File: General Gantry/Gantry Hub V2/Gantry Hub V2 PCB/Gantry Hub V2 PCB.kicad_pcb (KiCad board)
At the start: 4 copper layers, 140 x 85 mm, 44 parts, among them J1 Conn_01x02_Socket, J2 178-025-513R571, J3 DIN-8, J4 DIN-4, J5 DIN-4, J6 178-025-513R571, U1 TPIC6B595N, U10 TPIC6B595N, U11 TPIC6B595N, U12 TPIC6B595N, U13 TPIC6B595N, U2 SC0915, U3 LM2575-5.0WT, U4 TPIC6B595N, U5 LM358, U6 MCP4802, U7 SN74AHCT125N, U8 TPIC6B595N, U9 TPIC6B595N

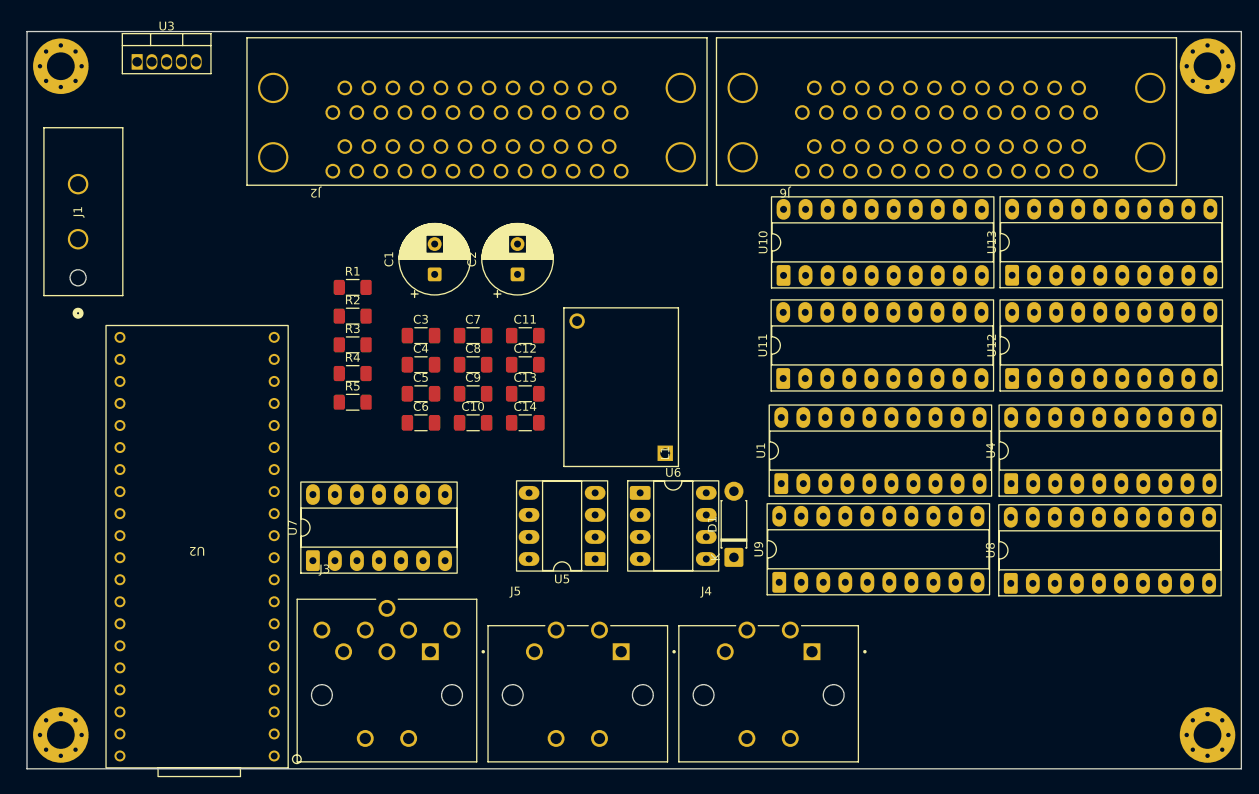
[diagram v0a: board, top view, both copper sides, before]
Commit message: Finalizes GH V2 part placement, about 60-75 percent done with routing
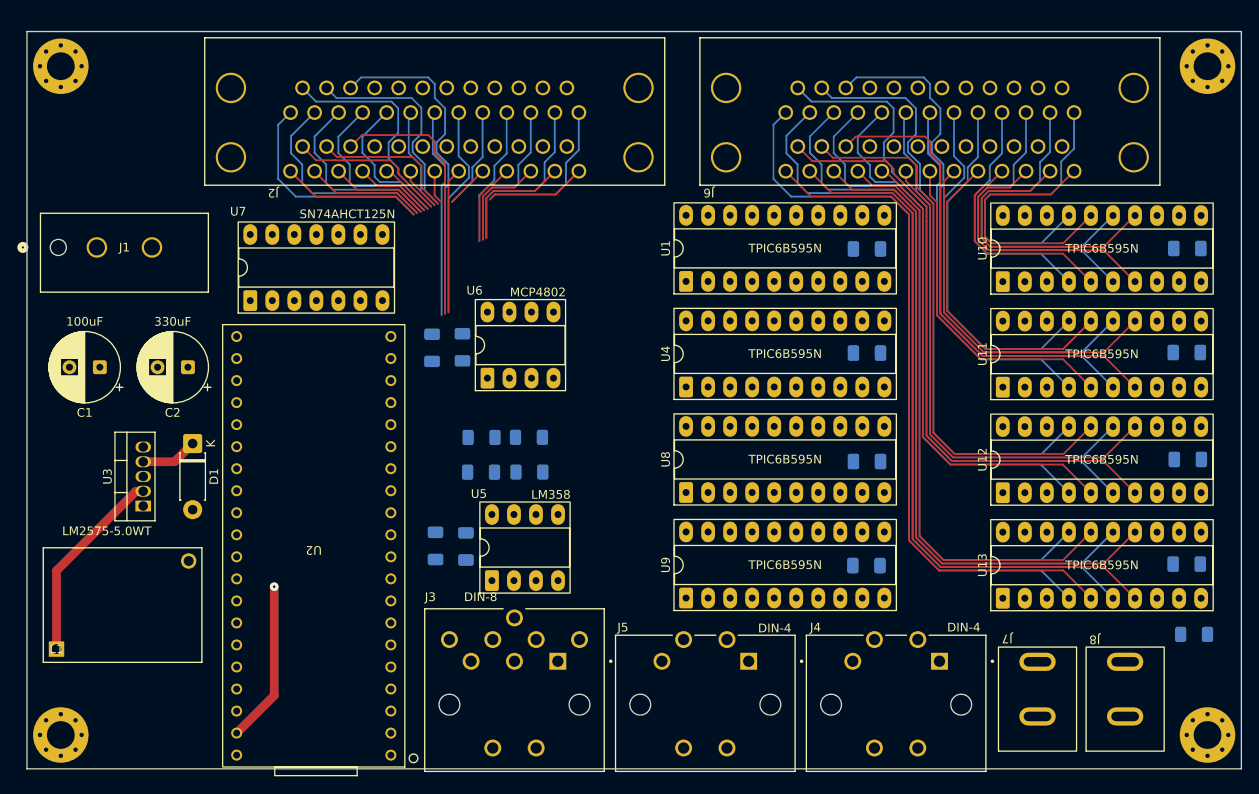
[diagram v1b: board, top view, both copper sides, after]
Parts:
- added J7: Barrel_Jack, lib_footprints:CUI PJ-037A, F.Cu at (172.5, 123.0)
- added J8: Barrel_Jack, lib_footprints:CUI PJ-037A, F.Cu at (182.6, 123.0)
- C10, C11, C12, C13, C14, C3, C4, C5, C6, C7, C8, C9, R1, R2, R3, R4, R5: moved to B.Cu
- moved R1 104.9 mm to (190.6, 113.5), turned to 180 degrees
- moved C14 78.0 mm to (189.7, 105.4), turned to 180 degrees
- moved C11 77.0 mm to (189.8, 69.0), turned to 180 degrees
- moved C13 76.8 mm to (189.8, 93.3), turned to 180 degrees
- moved C12 76.3 mm to (189.7, 81.0), turned to 180 degrees
- moved L1 73.7 mm to (59.4, 115.2), turned to 0 degrees
- moved D1 63.8 mm to (75.1, 91.5), turned to -90 degrees
- moved C3 52.4 mm to (152.8, 69.1), turned to 180 degrees
- moved C4 51.4 mm to (152.8, 81.1), turned to 180 degrees
- moved U3 51.2 mm to (69.4, 98.7), turned to 90 degrees
- moved C10 48.2 mm to (152.8, 105.6), turned to 180 degrees
- moved C9 46.1 mm to (152.8, 93.6), turned to 180 degrees
- moved C1 40.1 mm to (64.4, 82.7), turned to 180 degrees
- moved C2 39.5 mm to (74.6, 82.7), turned to 180 degrees
- moved U4 39.1 mm to (132.0, 85.0)
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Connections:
- U10 pad 14: /Valve Block Interface/CHANNEL_37 -> /Valve Block Interface/CHANNEL_44
- U10 pad 15: /Valve Block Interface/CHANNEL_38 -> /Valve Block Interface/CHANNEL_60
- U10 pad 16: /Valve Block Interface/CHANNEL_39 -> /Valve Block Interface/CHANNEL_45
- U10 pad 17: /Valve Block Interface/CHANNEL_40 -> /Valve Block Interface/CHANNEL_61
- U10 pad 4: /Valve Block Interface/CHANNEL_33 -> /Valve Block Interface/CHANNEL_58
- U10 pad 5: /Valve Block Interface/CHANNEL_34 -> /Valve Block Interface/CHANNEL_42
- U10 pad 6: /Valve Block Interface/CHANNEL_35 -> /Valve Block Interface/CHANNEL_59
- U10 pad 7: /Valve Block Interface/CHANNEL_36 -> /Valve Block Interface/CHANNEL_43
- U11 pad 14: /Valve Block Interface/CHANNEL_45 -> /Valve Block Interface/CHANNEL_40
- U11 pad 15: /Valve Block Interface/CHANNEL_46 -> /Valve Block Interface/CHANNEL_56
- U11 pad 16: /Valve Block Interface/CHANNEL_47 -> /Valve Block Interface/CHANNEL_41
- U11 pad 17: /Valve Block Interface/CHANNEL_48 -> /Valve Block Interface/CHANNEL_57
- U11 pad 4: /Valve Block Interface/CHANNEL_41 -> /Valve Block Interface/CHANNEL_55
- U11 pad 5: /Valve Block Interface/CHANNEL_42 -> /Valve Block Interface/CHANNEL_39
- U11 pad 6: /Valve Block Interface/CHANNEL_43 -> /Valve Block Interface/CHANNEL_64
- U11 pad 7: /Valve Block Interface/CHANNEL_44 -> /Valve Block Interface/CHANNEL_48
- U12 pad 14: /Valve Block Interface/CHANNEL_53 -> /Valve Block Interface/CHANNEL_38
- U12 pad 16: /Valve Block Interface/CHANNEL_55 -> /Valve Block Interface/CHANNEL_47
- U12 pad 17: /Valve Block Interface/CHANNEL_56 -> /Valve Block Interface/CHANNEL_63
- U12 pad 4: /Valve Block Interface/CHANNEL_49 -> /Valve Block Interface/CHANNEL_53
- U12 pad 5: /Valve Block Interface/CHANNEL_50 -> /Valve Block Interface/CHANNEL_37
- U12 pad 6: /Valve Block Interface/CHANNEL_51 -> /Valve Block Interface/CHANNEL_62
- U12 pad 7: /Valve Block Interface/CHANNEL_52 -> /Valve Block Interface/CHANNEL_46
- U13 pad 14: /Valve Block Interface/CHANNEL_61 -> /Valve Block Interface/CHANNEL_35
- U13 pad 15: /Valve Block Interface/CHANNEL_62 -> /Valve Block Interface/CHANNEL_51
- U13 pad 16: /Valve Block Interface/CHANNEL_63 -> /Valve Block Interface/CHANNEL_36
- U13 pad 17: /Valve Block Interface/CHANNEL_64 -> /Valve Block Interface/CHANNEL_52
- U13 pad 4: /Valve Block Interface/CHANNEL_57 -> /Valve Block Interface/CHANNEL_49
- U13 pad 5: /Valve Block Interface/CHANNEL_58 -> /Valve Block Interface/CHANNEL_33
- U13 pad 6: /Valve Block Interface/CHANNEL_59 -> /Valve Block Interface/CHANNEL_50
- U13 pad 7: /Valve Block Interface/CHANNEL_60 -> /Valve Block Interface/CHANNEL_34
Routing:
- net /Valve Block Interface/CHANNEL_50: track 0.00 -> 88.0 mm
- net /Valve Block Interface/CHANNEL_51: track 0.00 -> 85.1 mm
- net /Valve Block Interface/CHANNEL_49: track 0.00 -> 84.3 mm
- net /Valve Block Interface/CHANNEL_34: track 0.00 -> 79.9 mm
- net /Valve Block Interface/CHANNEL_33: track 0.00 -> 77.6 mm
- net /Valve Block Interface/CHANNEL_35: track 0.00 -> 77.0 mm
- net /Valve Block Interface/CHANNEL_52: track 0.00 -> 76.9 mm
- net /Valve Block Interface/CHANNEL_62: track 0.00 -> 76.5 mm
- net /Valve Block Interface/CHANNEL_46: track 0.00 -> 71.5 mm
- net /Valve Block Interface/CHANNEL_36: track 0.00 -> 68.8 mm
- net /Valve Block Interface/CHANNEL_63: track 0.00 -> 68.8 mm
- net /Valve Block Interface/CHANNEL_47: track 0.00 -> 63.9 mm
- net /Valve Block Interface/CHANNEL_53: track 0.00 -> 62.6 mm
- net /Valve Block Interface/CHANNEL_54: track 0.00 -> 62.1 mm
- net /Valve Block Interface/CHANNEL_64: track 0.00 -> 62.0 mm
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- added copper zone on In2.Cu, net +24V
- added copper zone on In2.Cu, net +5V
- added copper zone on In1.Cu, net GND

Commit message: Finishes V2.0 of gantry hub box
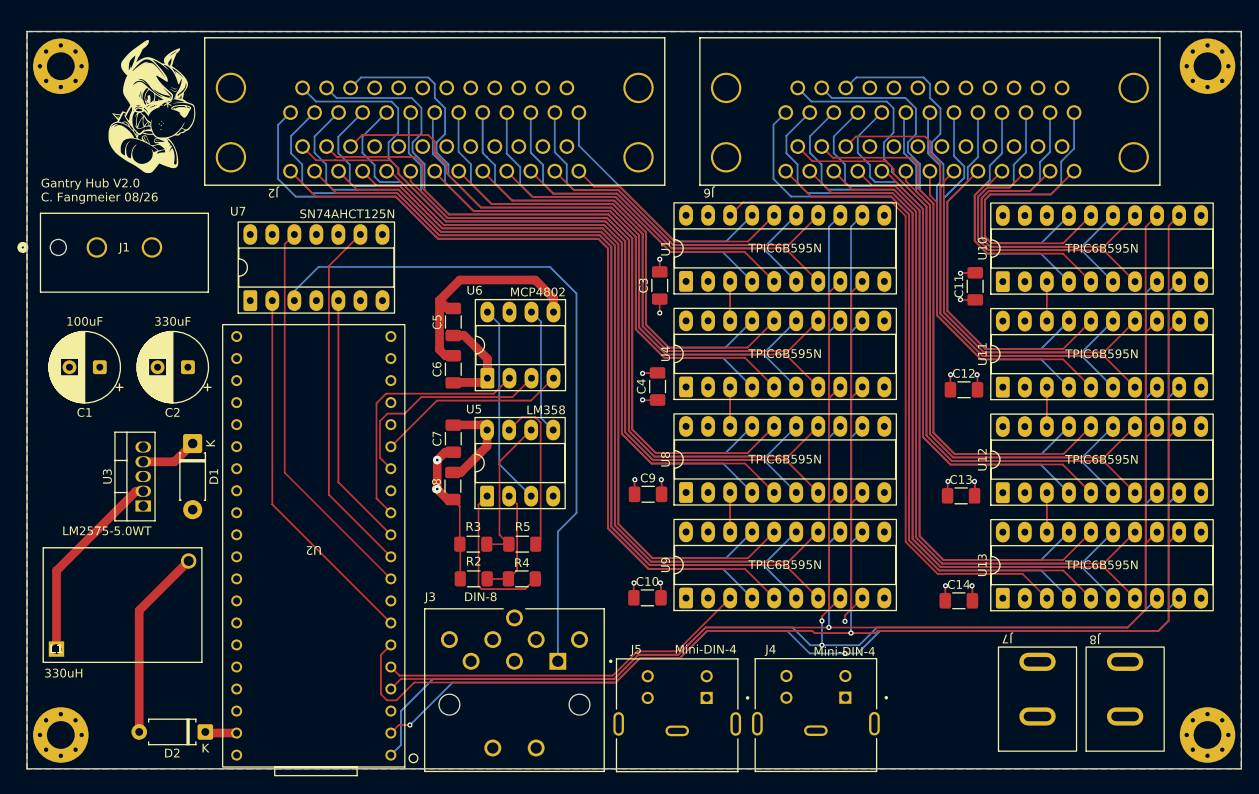
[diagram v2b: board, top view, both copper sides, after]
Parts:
- removed R1: 10k, Resistor_SMD:R_1206_3216Metric_Pad1.30x1.75mm_HandSolder
- added D2: 11DQ06, Diode_THT:D_A-405_P7.62mm_Horizontal, F.Cu at (76.6, 124.8)
- added G***: LOGO, lib_footprints:Rhett, F.Cu at (70.4, 52.6)
- C10, C11, C12, C13, C14, C3, C4, C5, C6, C7, C8, C9, R2, R3, R4, R5: moved to F.Cu
- J4, J5: value DIN-4 -> Mini-DIN-4; footprint lib_footprints:CUI_SDF-40J -> lib_footprints:CUI_MD-40SM
- moved C14 26.6 mm to (163.4, 109.6), turned to 0 degrees
- moved C13 26.5 mm to (163.7, 97.5), turned to 0 degrees
- moved C12 26.0 mm to (164.0, 85.3), turned to 0 degrees
- moved C9 25.5 mm to (127.6, 97.3), turned to 0 degrees
- moved C10 25.5 mm to (127.5, 109.3), turned to 0 degrees
- moved C11 24.8 mm to (165.3, 73.4), turned to 90 degrees
- moved C4 24.4 mm to (128.7, 84.9), turned to 90 degrees
- moved C3 24.3 mm to (128.9, 73.3), turned to 90 degrees
- moved R2 13.9 mm to (107.5, 107.1), turned to 180 degrees
- moved R3 13.9 mm to (107.5, 103.1), turned to 180 degrees
- moved R4 13.2 mm to (113.0, 107.1), turned to 0 degrees
- moved R5 13.2 mm to (113.1, 103.1), turned to 0 degrees
- moved C7 12.5 mm to (105.2, 90.9)
- moved U5 9.76 mm to (109.0, 97.6)
- moved J4 9.72 mm to (146.9, 124.6)
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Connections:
- J4 pad 2: /Root/ANALOG_OUT_1 -> /Root/ANALOG_OUT_2
- J5 pad 2: /Root/ANALOG_OUT_2 -> /Root/ANALOG_OUT_1
- U1 pad 12: /Valve Block Interface/RCK -> MNFLD-R_{CK}
- U1 pad 13: /Valve Block Interface/SRCK -> MNFLD-S_{CK}
- U1 pad 14: /Valve Block Interface/CHANNEL_05 -> /Valve Block Interface/CHANNEL_12
- U1 pad 15: /Valve Block Interface/CHANNEL_06 -> /Valve Block Interface/CHANNEL_28
- U1 pad 16: /Valve Block Interface/CHANNEL_07 -> /Valve Block Interface/CHANNEL_13
- U1 pad 17: /Valve Block Interface/CHANNEL_08 -> /Valve Block Interface/CHANNEL_29
- U1 pad 18: Net-(U1-SEROUT) -> /Valve Block Interface/MNFLD-S_{4}
- U1 pad 3: /Valve Block Interface/SERIN_0 -> /Valve Block Interface/MNFLD-S_{3}
- U1 pad 4: /Valve Block Interface/CHANNEL_01 -> /Valve Block Interface/CHANNEL_26
- U1 pad 5: /Valve Block Interface/CHANNEL_02 -> /Valve Block Interface/CHANNEL_10
- U1 pad 6: /Valve Block Interface/CHANNEL_03 -> /Valve Block Interface/CHANNEL_27
- U1 pad 7: /Valve Block Interface/CHANNEL_04 -> /Valve Block Interface/CHANNEL_11
- U1 pad 8: /Valve Block Interface/~{SRCLR} -> MNFLD-~{SRCLR}
- U1 pad 9: /Valve Block Interface/VALVE~{G} -> MNFLD-DISABLE
- U10 pad 12: /Valve Block Interface/RCK -> MNFLD-R_{CK}
- U10 pad 13: /Valve Block Interface/SRCK -> MNFLD-S_{CK}
- U10 pad 18: Net-(U10-SEROUT) -> unconnected-(U10-SEROUT-Pad18)
- U10 pad 3: /Valve Block Interface/SERCONN_1 -> /Valve Block Interface/MNFLD-S_{7}
- U10 pad 8: /Valve Block Interface/~{SRCLR} -> MNFLD-~{SRCLR}
- U10 pad 9: /Valve Block Interface/VALVE~{G} -> MNFLD-DISABLE
- U11 pad 12: /Valve Block Interface/RCK -> MNFLD-R_{CK}
- U11 pad 13: /Valve Block Interface/SRCK -> MNFLD-S_{CK}
- U11 pad 18: /Valve Block Interface/SERCONN_2 -> /Valve Block Interface/MNFLD-S_{7}
- U11 pad 3: Net-(U10-SEROUT) -> /Valve Block Interface/MNFLD-S_{6}
- U11 pad 8: /Valve Block Interface/~{SRCLR} -> MNFLD-~{SRCLR}
- U11 pad 9: /Valve Block Interface/VALVE~{G} -> MNFLD-DISABLE
- U12 pad 12: /Valve Block Interface/RCK -> MNFLD-R_{CK}
- U12 pad 13: /Valve Block Interface/SRCK -> MNFLD-S_{CK}
- U12 pad 18: Net-(U12-SEROUT) -> /Valve Block Interface/MNFLD-S_{6}
- U12 pad 3: /Valve Block Interface/SERCONN_2 -> /Valve Block Interface/MNFLD-S_{5}
- U12 pad 8: /Valve Block Interface/~{SRCLR} -> MNFLD-~{SRCLR}
- U12 pad 9: /Valve Block Interface/VALVE~{G} -> MNFLD-DISABLE
- U13 pad 12: /Valve Block Interface/RCK -> MNFLD-R_{CK}
- U13 pad 13: /Valve Block Interface/SRCK -> MNFLD-S_{CK}
- U13 pad 18: /Valve Block Interface/SEROUT -> /Valve Block Interface/MNFLD-S_{5}
- U13 pad 3: Net-(U12-SEROUT) -> /Valve Block Interface/MNFLD-S_{4}
- U13 pad 8: /Valve Block Interface/~{SRCLR} -> MNFLD-~{SRCLR}
- U13 pad 9: /Valve Block Interface/VALVE~{G} -> MNFLD-DISABLE
- U2 pad 1: unconnected-(U2-UART0_TX/I2C0_SDA/SPI0_RX/GP0-Pad1) -> MNFLD-~{SRCLR}
- U2 pad 10: unconnected-(U2-I2C1_SCL/SPI0_TX/GP7-Pad10) -> /Root/D2
- U2 pad 11: unconnected-(U2-UART1_TX/I2C0_SDA/SPI1_RX/GP8-Pad11) -> /Root/D1
- U2 pad 12: unconnected-(U2-UART1_RX/I2C0_SCL/SPI1_CSn/GP9-Pad12) -> /Root/DAC_~{CS}
- U2 pad 14: unconnected-(U2-I2C1_SDA/SPI1_SCK/GP10-Pad14) -> /Root/DAC_{SCK}
- U2 pad 15: unconnected-(U2-I2C1_SCL/SPI1_TX/GP11-Pad15) -> /Root/DAC_{SDI}
- U2 pad 2: unconnected-(U2-UART0_RX/I2C0_SCL/GPI0_CSn/GP1-Pad2) -> MNFLD-DISABLE
- U2 pad 39: +5V -> Net-(D2-K)
- U2 pad 4: unconnected-(U2-I2C1_SDA/SPI0_SCK/GP2-Pad4) -> MNFLD-S_{CK}
- U2 pad 5: unconnected-(U2-I2C1_SCL/SPI0_TX/GP3-Pad5) -> MNFLD-S_{IN}
- U2 pad 6: unconnected-(U2-UART1_TX/I2C0_SDA/SPI0_RX/GP4-Pad6) -> MNFLD-R_{CK}
- U2 pad 7: unconnected-(U2-UART1_RX/I2C0_SCL/SPI0_CSn/GP5-Pad7) -> /Root/D0
- U2 pad 9: unconnected-(U2-I2C1_SDA/SPI0_SCK/GP6-Pad9) -> /Root/D3
- U4 pad 12: /Valve Block Interface/RCK -> MNFLD-R_{CK}
- U4 pad 13: /Valve Block Interface/SRCK -> MNFLD-S_{CK}
- U4 pad 14: /Valve Block Interface/CHANNEL_13 -> /Valve Block Interface/CHANNEL_08
- U4 pad 15: /Valve Block Interface/CHANNEL_14 -> /Valve Block Interface/CHANNEL_24
- U4 pad 16: /Valve Block Interface/CHANNEL_15 -> /Valve Block Interface/CHANNEL_09
- U4 pad 17: /Valve Block Interface/CHANNEL_16 -> /Valve Block Interface/CHANNEL_25
- U4 pad 18: /Valve Block Interface/SERCONN_0 -> /Valve Block Interface/MNFLD-S_{3}
- U4 pad 3: Net-(U1-SEROUT) -> /Valve Block Interface/MNFLD-S_{2}
- U4 pad 4: /Valve Block Interface/CHANNEL_09 -> /Valve Block Interface/CHANNEL_23
- U4 pad 5: /Valve Block Interface/CHANNEL_10 -> /Valve Block Interface/CHANNEL_07
- U4 pad 6: /Valve Block Interface/CHANNEL_11 -> /Valve Block Interface/CHANNEL_32
- U4 pad 7: /Valve Block Interface/CHANNEL_12 -> /Valve Block Interface/CHANNEL_16
- U4 pad 8: /Valve Block Interface/~{SRCLR} -> MNFLD-~{SRCLR}
- U4 pad 9: /Valve Block Interface/VALVE~{G} -> MNFLD-DISABLE
- U6 pad 3: /Root/SPI_SCK -> /Root/DAC_{SCK}
- U6 pad 4: /Root/SPI_SDI -> /Root/DAC_{SDI}
- U7 pad 12: unconnected-(U7-4A-Pad12) -> /Root/D3
- U7 pad 2: /Root/DISPENSE_ENABLE -> /Root/D0
- U7 pad 5: unconnected-(U7-2A-Pad5) -> /Root/D1
- U7 pad 9: unconnected-(U7-3A-Pad9) -> /Root/D2
- U8 pad 12: /Valve Block Interface/RCK -> MNFLD-R_{CK}
- U8 pad 13: /Valve Block Interface/SRCK -> MNFLD-S_{CK}
- U8 pad 14: /Valve Block Interface/CHANNEL_21 -> /Valve Block Interface/CHANNEL_06
- U8 pad 16: /Valve Block Interface/CHANNEL_23 -> /Valve Block Interface/CHANNEL_15
- U8 pad 17: /Valve Block Interface/CHANNEL_24 -> /Valve Block Interface/CHANNEL_31
- U8 pad 18: Net-(U8-SEROUT) -> /Valve Block Interface/MNFLD-S_{2}
- U8 pad 3: /Valve Block Interface/SERCONN_0 -> /Valve Block Interface/MNFLD-S_{1}
- U8 pad 4: /Valve Block Interface/CHANNEL_17 -> /Valve Block Interface/CHANNEL_21
- U8 pad 5: /Valve Block Interface/CHANNEL_18 -> /Valve Block Interface/CHANNEL_05
- U8 pad 6: /Valve Block Interface/CHANNEL_19 -> /Valve Block Interface/CHANNEL_30
- U8 pad 7: /Valve Block Interface/CHANNEL_20 -> /Valve Block Interface/CHANNEL_14
- U8 pad 8: /Valve Block Interface/~{SRCLR} -> MNFLD-~{SRCLR}
- U8 pad 9: /Valve Block Interface/VALVE~{G} -> MNFLD-DISABLE
- U9 pad 12: /Valve Block Interface/RCK -> MNFLD-R_{CK}
- U9 pad 13: /Valve Block Interface/SRCK -> MNFLD-S_{CK}
- U9 pad 14: /Valve Block Interface/CHANNEL_29 -> /Valve Block Interface/CHANNEL_03
- U9 pad 15: /Valve Block Interface/CHANNEL_30 -> /Valve Block Interface/CHANNEL_19
- U9 pad 16: /Valve Block Interface/CHANNEL_31 -> /Valve Block Interface/CHANNEL_04
- U9 pad 17: /Valve Block Interface/CHANNEL_32 -> /Valve Block Interface/CHANNEL_20
- U9 pad 18: /Valve Block Interface/SERCONN_1 -> /Valve Block Interface/MNFLD-S_{1}
- U9 pad 3: Net-(U8-SEROUT) -> MNFLD-S_{IN}
- U9 pad 4: /Valve Block Interface/CHANNEL_25 -> /Valve Block Interface/CHANNEL_17
- U9 pad 5: /Valve Block Interface/CHANNEL_26 -> /Valve Block Interface/CHANNEL_01
- U9 pad 6: /Valve Block Interface/CHANNEL_27 -> /Valve Block Interface/CHANNEL_18
- U9 pad 7: /Valve Block Interface/CHANNEL_28 -> /Valve Block Interface/CHANNEL_02
- U9 pad 8: /Valve Block Interface/~{SRCLR} -> MNFLD-~{SRCLR}
- U9 pad 9: /Valve Block Interface/VALVE~{G} -> MNFLD-DISABLE
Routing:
- net MNFLD-R_{CK}: track 0.00 -> 208.3 mm, vias 0 -> 1
- net MNFLD-S_{CK}: track 0.00 -> 195.9 mm, vias 0 -> 1
- net MNFLD-DISABLE: track 0.00 -> 191.0 mm, vias 0 -> 3
- net MNFLD-~{SRCLR}: track 0.00 -> 190.1 mm, vias 0 -> 2
- net /Valve Block Interface/CHANNEL_02: track 13.9 -> 97.4 mm
- net /Valve Block Interface/CHANNEL_03: track 11.4 -> 94.3 mm
- net /Valve Block Interface/CHANNEL_18: track 24.5 -> 105.4 mm
- net /Valve Block Interface/CHANNEL_19: track 22.1 -> 102.4 mm
- net /Root/DISPENSE_ENABLE_OUT: track 0.00 -> 79.3 mm
- net /Valve Block Interface/CHANNEL_01: track 16.3 -> 95.1 mm
- net /Valve Block Interface/MNFLD-S_{4}: track 0.00 -> 78.1 mm
- net /Valve Block Interface/CHANNEL_04: track 8.98 -> 86.1 mm
- net /Valve Block Interface/CHANNEL_17: track 25.6 -> 101.8 mm
- net /Valve Block Interface/CHANNEL_20: track 19.7 -> 94.3 mm
- net /Valve Block Interface/CHANNEL_14: track 18.4 -> 89.6 mm
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- added copper zone on B.Cu, net (none)
- added copper zone on F.Cu, net (none)
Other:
- board text added: "Gantry Hub V2.0 C. Fangmeier 08/26"
- board text added: "Scan me for design files!"
